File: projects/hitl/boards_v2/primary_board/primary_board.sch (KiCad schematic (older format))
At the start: 76 parts, among them J1 USB-Micro-1981568-1, J11 CONN_01X03, J12 CONN_01X03, J13 CONN_01X03, J14 CONN_01X03, J15 CONN_01X03, J16 CONN_01X03, J17 CONN_01x02, J2 Barrel_jack, J3 DSub-9, J4 SSW-122-01-G-D, J5 MM_F_VT_06_SM, J6 MM_F_VT_06_SM, Q1 SSM3K333R, Q2 SSM3K333R, Q3 SSM3K333R, Q4 SSM3K333R, U1 R_500, U2 FT4222H, U3 PCA9306, U4 AD5675, U5 MAX7300AAXT, Y1 Crystal_12MHz

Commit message: replaced ADC and micromatch. Add 0-ohm resistors to power
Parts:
- removed J5, J6: MM_F_VT_06_SM, footprints:micromatch_female_vert_6_sm, symbol formula:MM_F_VT_06_SM
- added C17: C_10uF_16V, footprints:C_0805_OEM, symbol formula:C_10uF_16V
- added J13, J15: CONN_01x02, footprints:PinHeader_1x02_P2.54mm_Vertical, symbol formula:CONN_01x02
- added J3, J4: MM_F_VT_08_SM, footprints:micromatch_female_vert_8_sm, symbol formula:MM_F_VT_08_SM
- added R44, R45: R_0, footprints:R_0603_1608Metric, symbol formula:R_0
- renumbered C24 to C15, C15 to C16, C16 to C18, C17 to C19, J12 to J10, J15 to J11, J16 to J12, J4 to J14, J17 to J5, J3 to J6, J13 to J7, J14 to J8, J11 to J9
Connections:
- net labels added: CAN_AWAY+, CAN_AWAY-
- net labels removed: Analog-MUX8
- wire segments 383 -> 398
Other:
- note added: "Address Start:\n030......"
- note added: "Away From Primary"
- note added: "Towards Primary"

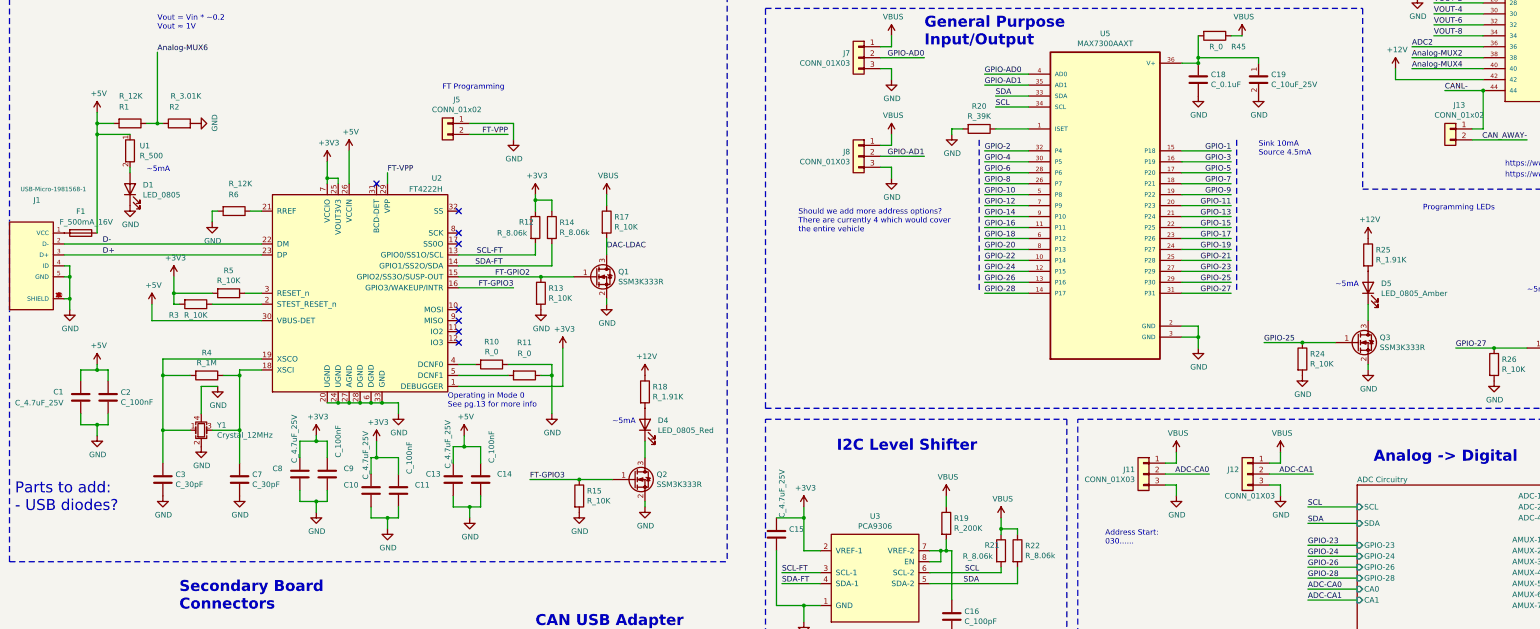
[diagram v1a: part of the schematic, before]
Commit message: Update passives. Update floorplan
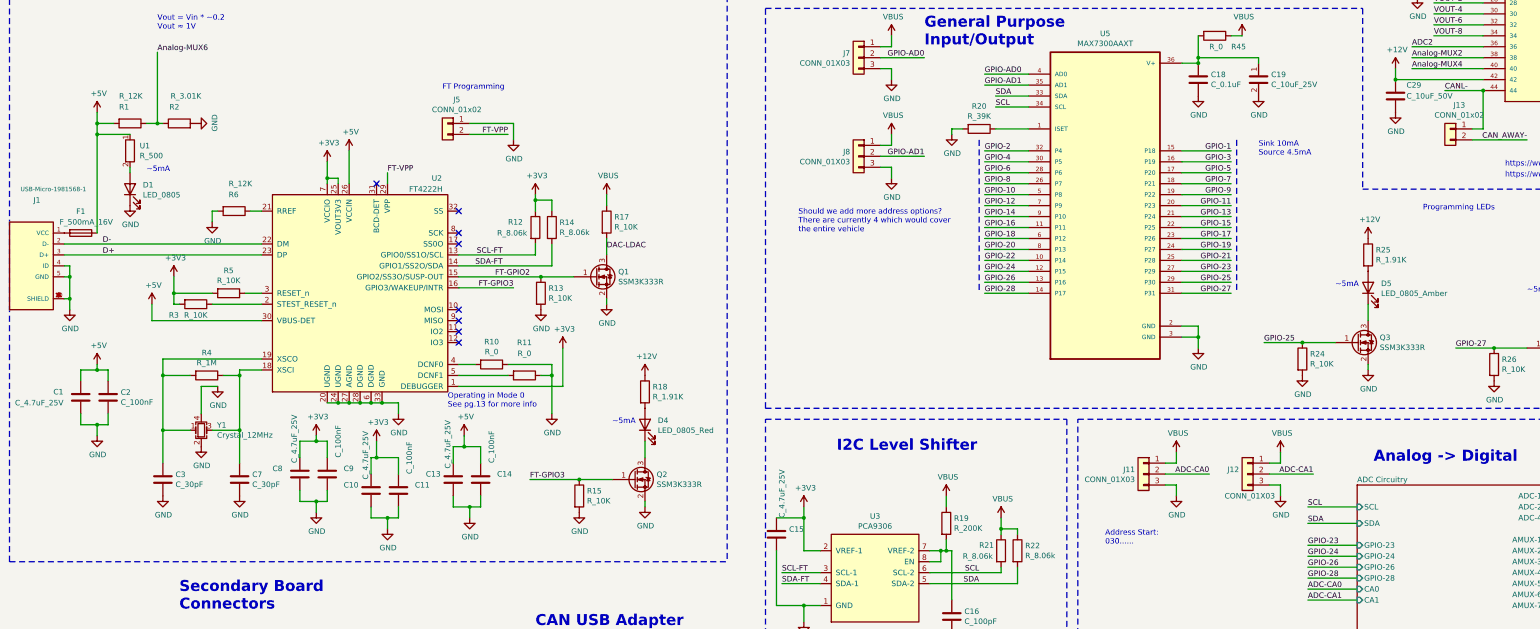
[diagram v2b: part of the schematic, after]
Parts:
- added C29: C_10uF_50V, footprints:C_0805_OEM, symbol formula:C_10uF_50V
- J13, J15, J5: footprint footprints:PinHeader_1x02_P2.54mm_Vertical -> footprints:pinheader_1x2
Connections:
- net +12V: now also C29.1
- net GND: now also C29.2
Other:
- note removed: "Parts to add:\n- USB diodes?"
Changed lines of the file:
@@
 Wire Wire Line
 	1900 6200 1900 6050
-Text Notes 650  7950 0    100  ~ 0
-Parts to add:\n- USB diodes?
 $Comp
 L formula:C_4.7uF_25V C1
@@
 U 1 1 612CC8D8
 P 5400 5350
-F 0 "R12" H 5250 5400 50  0000 L CNN
+F 0 "R12" H 5150 5400 50  0000 L CNN
 F 1 "R_8.06k" H 5050 5300 50  0000 L CNN
 F 2 "footprints:R_0805_OEM" H 5330 5850 50  0001 C CNN
@@
 F 0 "J5" H 4518 4617 50  0000 C CNN
 F 1 "CONN_01x02" H 4518 4526 50  0000 C CNN
-F 2 "footprints:PinHeader_1x02_P2.54mm_Vertical" H 4500 4400 50  0001 C CNN
+F 2 "footprints:pinheader_1x2" H 4500 4400 50  0001 C CNN
 F 3 "https://katalog.we-online.de/em/datasheet/6130xx11121.pdf" H 4600 4500 50  0001 C CNN
 F 4 "DK" H 4700 4600 50  0001 C CNN "MFN"
@@
 U 1 1 613E36EF
 P 9650 8300
-F 0 "R21" H 9500 8350 50  0000 L CNN
+F 0 "R21" H 9450 8350 50  0000 L CNN
 F 1 "R_8.06k" H 9300 8250 50  0000 L CNN
 F 2 "footprints:R_0805_OEM" H 9580 8800 50  0001 C CNN
@@
 F 0 "J13" H 13668 4667 50  0000 C CNN
 F 1 "CONN_01x02" H 13668 4576 50  0000 C CNN
-F 2 "footprints:PinHeader_1x02_P2.54mm_Vertical" H 13650 4450 50  0001 C CNN
+F 2 "footprints:pinheader_1x2" H 13650 4450 50  0001 C CNN
 F 3 "https://katalog.we-online.de/em/datasheet/6130xx11121.pdf" H 13750 4550 50  0001 C CNN
 F 4 "DK" H 13850 4650 50  0001 C CNN "MFN"
@@
 F 0 "J15" H 14668 4667 50  0000 C CNN
 F 1 "CONN_01x02" H 14668 4576 50  0000 C CNN
-F 2 "footprints:PinHeader_1x02_P2.54mm_Vertical" H 14650 4450 50  0001 C CNN
+F 2 "footprints:pinheader_1x2" H 14650 4450 50  0001 C CNN
 F 3 "https://katalog.we-online.de/em/datasheet/6130xx11121.pdf" H 14750 4550 50  0001 C CNN
 F 4 "DK" H 14850 4650 50  0001 C CNN "MFN"
@@
 Wire Wire Line
 	11450 3600 11450 3800
+$Comp
+L formula:C_10uF_50V C29
+U 1 1 626AD773
+P 13250 4200
+F 0 "C29" H 13350 4350 50  0000 L CNN
+F 1 "C_10uF_50V" H 13350 4250 50  0000 L CNN
+F 2 "footprints:C_0805_OEM" H 13288 4800 50  0001 C CNN
+F 3 "http://www.samsungsem.com/kr/support/product-https://search.murata.co.jp/Ceramy/image/img/A01X/G101/ENG/GRM21BR61H106KE43-01A.pdf" H 13275 5050 50  0001 C CNN
+F 4 "Murata" H 13250 4250 60  0001 C CNN "MFN"
+F 5 "GRM21BR61H106KE43L" H 13250 4950 60  0001 C CNN "MPN"
+F 6 "https://www.digikey.com/en/products/detail/murata-electronics/GRM21BR61H106KE43L/10326316" H 13675 4700 60  0001 C CNN "PurchasingLink"
+	1    13250 4200
+	1    0    0    -1
+$EndComp
+Connection ~ 13250 4000
+$Comp
+L power:GND #PWR?
+U 1 1 626AE047
+P 13250 4300
+F 0 "#PWR?" H 13250 4050 50  0001 C CNN
+F 1 "GND" H 13255 4127 50  0000 C CNN
+F 2 "" H 13250 4300 50  0001 C CNN
+F 3 "" H 13250 4300 50  0001 C CNN
+	1    13250 4300
+	1    0    0    -1
+$EndComp
 $EndSCHEMATC
